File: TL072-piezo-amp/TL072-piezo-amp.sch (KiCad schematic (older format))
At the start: 9 parts

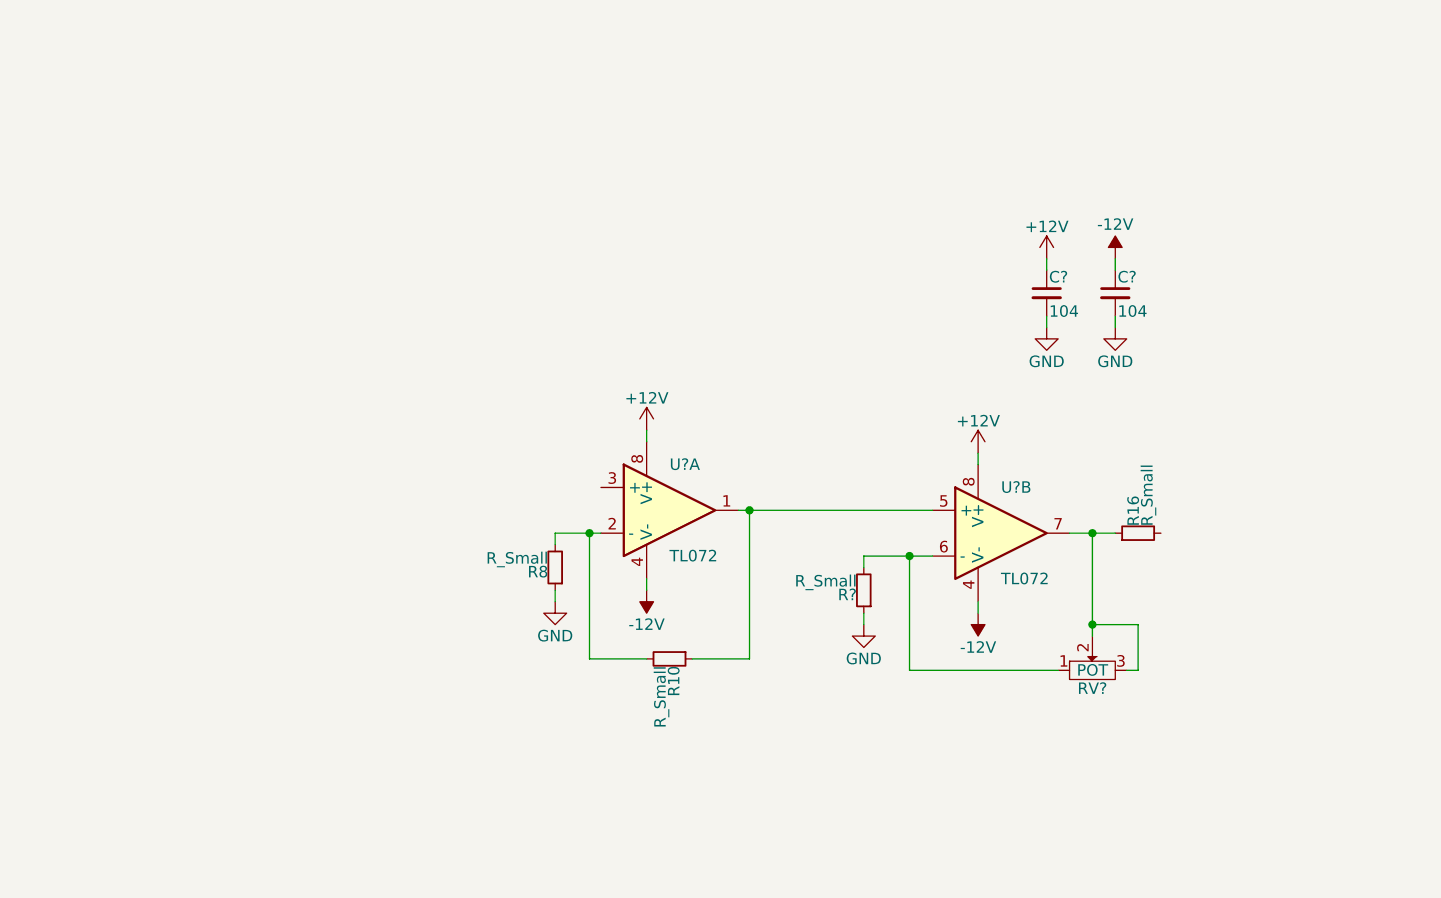
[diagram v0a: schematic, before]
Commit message: Finalize TL072-piezo-amp schematic
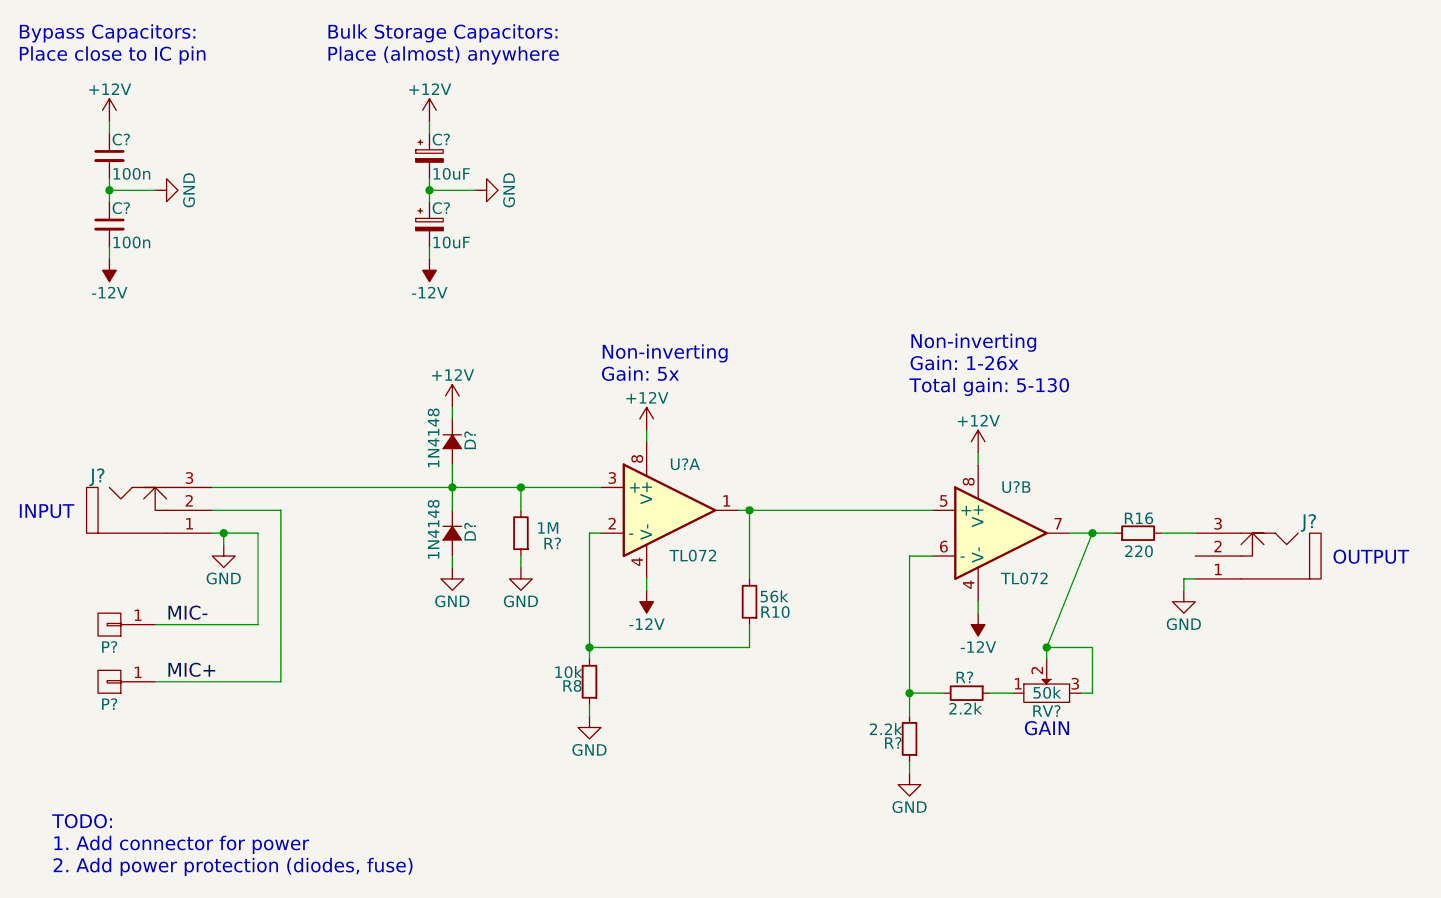
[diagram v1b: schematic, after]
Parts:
- removed C?: 104, symbol C_Small
- added C? (x2): 10uF, symbol CP_Small
- added C?: 100n, symbol C_Small
- added D? (x2): 1N4148, symbol D_Small
- added J? (x2): 3.5mm_mono_switched_jack_PJ-301B, symbol 3.5mm_mono_switched_jack_PJ-301B
- added P? (x2): CONN_01X01, symbol CONN_01X01
- added R?: 2.2k, symbol R_Small
- added R?: 1M, symbol R_Small
- C?: value 104 -> 100n
- R10: value R_Small -> 56k
- R16: value R_Small -> 220
- R8: value R_Small -> 10k
- R?: value R_Small -> 2.2k
- RV?: value POT -> 50k
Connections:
- net +12V: now also C?.1, D?.1 (K)
- net -12V: now also C?.2, C?.2
- net GND: now also C?.1, C?.1, C?.2, D?.2 (A), J?.1, J?.1, P?.1 (P1), R?.1
- net at U?.1, U?.5 (+): now also R10.2; no longer R10.1
- net at R8.2, U?.2 (-): now also R10.1; no longer R10.2
- net at U?.3 (+): now also D?.1 (K), D?.2 (A), J?.3, R?.2
- net at R?.2, U?.6 (-): now also R?.2; no longer RV?.1
- net at R16.2: now also J?.3
- new net: R?.1, RV?.1
- new net MIC+: J?.2, P?.1 (P1)
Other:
- note added: "Bulk Storage Capacitors:\nPlace (almost) anywhere"
- note added: "Bypass Capacitors:\nPlace close to IC pin"
- note added: "GAIN"
- note added: "INPUT"
- note added: "Non-inverting\nGain: 1-26x\nTotal gain: 5-130"
- note added: "Non-inverting\nGain: 5x"
- note added: "OUTPUT"
- note added: "TODO:\n1. Add connector for power\n2. Add power protection (diodes, fuse)"
- moved on the sheet: C?, R10, R8, R?, RV?
